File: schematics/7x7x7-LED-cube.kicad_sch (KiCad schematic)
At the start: 513 parts, among them Q1 PN2222A, Q10 PN2222A, Q11 PN2222A, Q12 PN2222A, Q13 PN2222A, Q14 PN2222A, Q15 PN2222A, Q16 PN2222A, Q17 PN2222A, Q18 PN2222A, Q19 PN2222A, Q2 PN2222A, Q20 PN2222A, Q21 PN2222A, Q22 PN2222A, Q23 PN2222A, Q24 PN2222A, Q25 PN2222A, Q26 PN2222A, Q27 PN2222A, Q28 PN2222A, Q29 PN2222A, Q3 PN2222A, Q30 PN2222A, Q31 PN2222A, Q32 PN2222A, Q33 PN2222A, Q34 PN2222A, Q35 PN2222A, Q36 PN2222A, Q37 PN2222A, Q38 PN2222A, Q39 PN2222A, Q4 PN2222A, Q40 PN2222A, Q41 PN2222A, Q42 PN2222A, Q43 PN2222A, Q44 PN2222A, Q45 PN2222A, Q46 PN2222A, Q47 PN2222A, Q48 PN2222A, Q49 PN2222A, Q5 PN2222A, Q6 PN2222A, Q7 PN2222A, Q8 PN2222A, Q9 PN2222A, SW1 SW_Push, U1 FQP30N06L, U2 FQP30N06L, U3 FQP30N06L, U4 FQP30N06L, U5 FQP30N06L, U6 FQP30N06L, U7 FQP30N06L

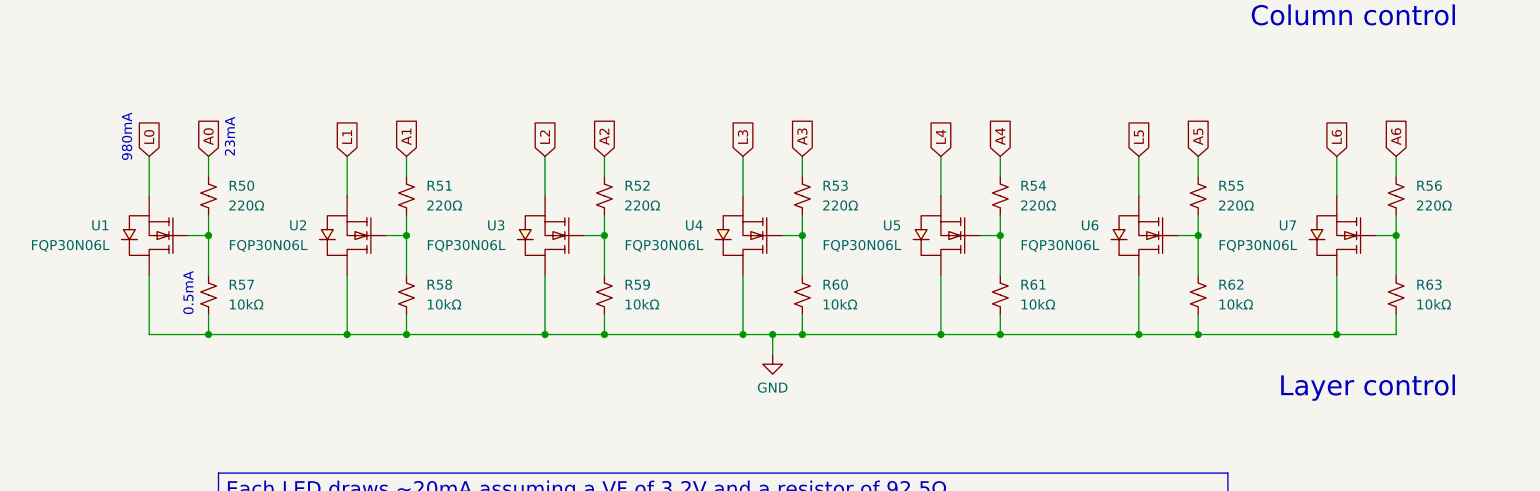
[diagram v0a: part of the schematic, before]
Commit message: fix(schematic): swap MOSFET source/drain
There needs to be a potential between the gate and source in order to activate, otherwise it won't turn on and will just leak constantly through the internal diode.
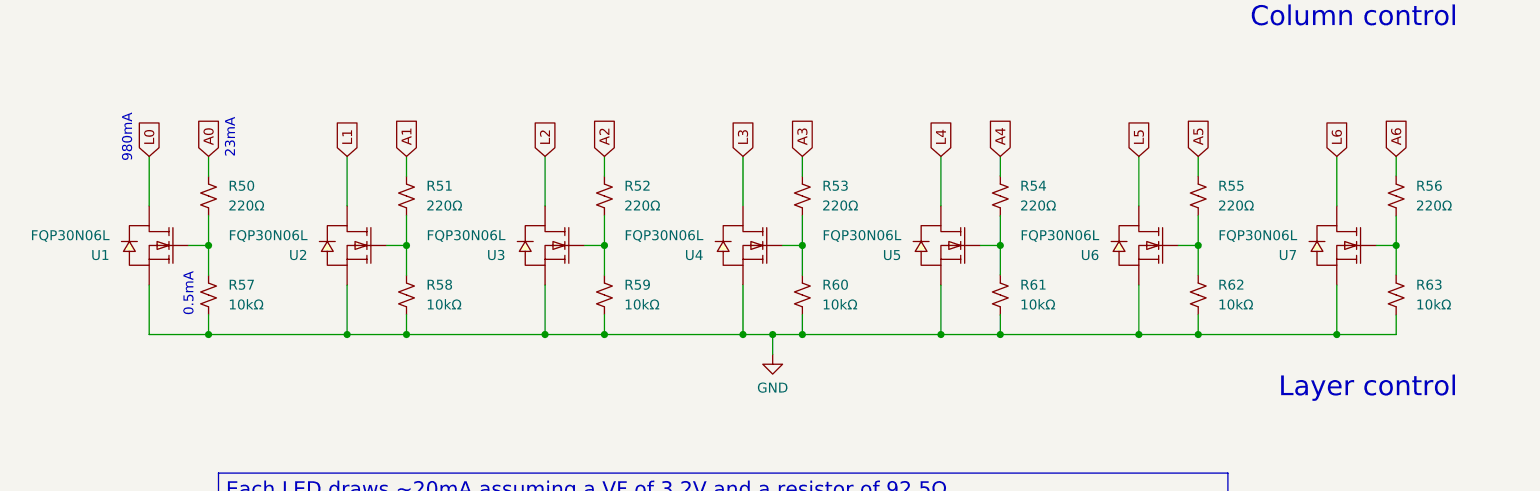
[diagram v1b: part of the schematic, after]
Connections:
- net GND: now also U1.3 (S), U2.3 (S), U3.3 (S), U4.3 (S), U5.3 (S), U6.3 (S), U7.3 (S); no longer U1.2 (D), U2.2 (D), U3.2 (D), U4.2 (D), U5.2 (D), U6.2 (D), U7.2 (D)
- net L0: now also U1.2 (D); no longer U1.3 (S)
- net L1: now also U2.2 (D); no longer U2.3 (S)
- net L2: now also U3.2 (D); no longer U3.3 (S)
- net L3: now also U4.2 (D); no longer U4.3 (S)
- net L4: now also U5.2 (D); no longer U5.3 (S)
- net L5: now also U6.2 (D); no longer U6.3 (S)
- net L6: now also U7.2 (D); no longer U7.3 (S)
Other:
- moved on the sheet: U1, U2, U3, U4, U5, U6, U7

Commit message: fix: various wiring issues
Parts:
- added REF1: 16V2200uf_10X20, footprint:CAP-TH_BD10.0-P5.00-D1.0-FD, symbol 16V2200uf_10X20:16V2200uf_10X20
- R1, R10, R11, R12, R13, R14, R15, R16, R17, R18, R19, R2, R20, R21, R22, R23, R24, R25, R26, R27, R28, R29, R3, R30, R31, R32, R33, R34, R35, R36, R37, R38, R39, R4, R40, R41, R42, R43, R44, R45, R46, R47, R48, R49, R5, R6, R7, R8, R9: value 92Ω -> 82Ω
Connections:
- net +5V: now also A1.5V1 (5V), REF1.1; no longer A1.5V4 (5V)
- net GND: now also REF1.2
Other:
- note added: "Controller"
- moved on the sheet: A1, SW1
